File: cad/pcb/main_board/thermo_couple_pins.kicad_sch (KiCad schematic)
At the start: 3 parts

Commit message: Thermo Couple Pins
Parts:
- removed R3, R4: R, symbol Device:R
- removed TC1: 0-60V, symbol Device:Thermocouple_Block
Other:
- added sheet TCPin (tcpin.kicad_sch)
- added sheet TCPin1 (tcpin.kicad_sch)
- added sheet TCPin10 (tcpin.kicad_sch)
- added sheet TCPin11 (tcpin.kicad_sch)
- added sheet TCPin12 (tcpin.kicad_sch)
- added sheet TCPin13 (tcpin.kicad_sch)
- added sheet TCPin14 (tcpin.kicad_sch)
- added sheet TCPin15 (tcpin.kicad_sch)
- added sheet TCPin2 (tcpin.kicad_sch)
- added sheet TCPin3 (tcpin.kicad_sch)
- added sheet TCPin4 (tcpin.kicad_sch)
- added sheet TCPin5 (tcpin.kicad_sch)
- added sheet TCPin6 (tcpin.kicad_sch)
- added sheet TCPin7 (tcpin.kicad_sch)
- added sheet TCPin8 (tcpin.kicad_sch)
- added sheet TCPin9 (tcpin.kicad_sch)
- note removed: "Cap for low pass?"

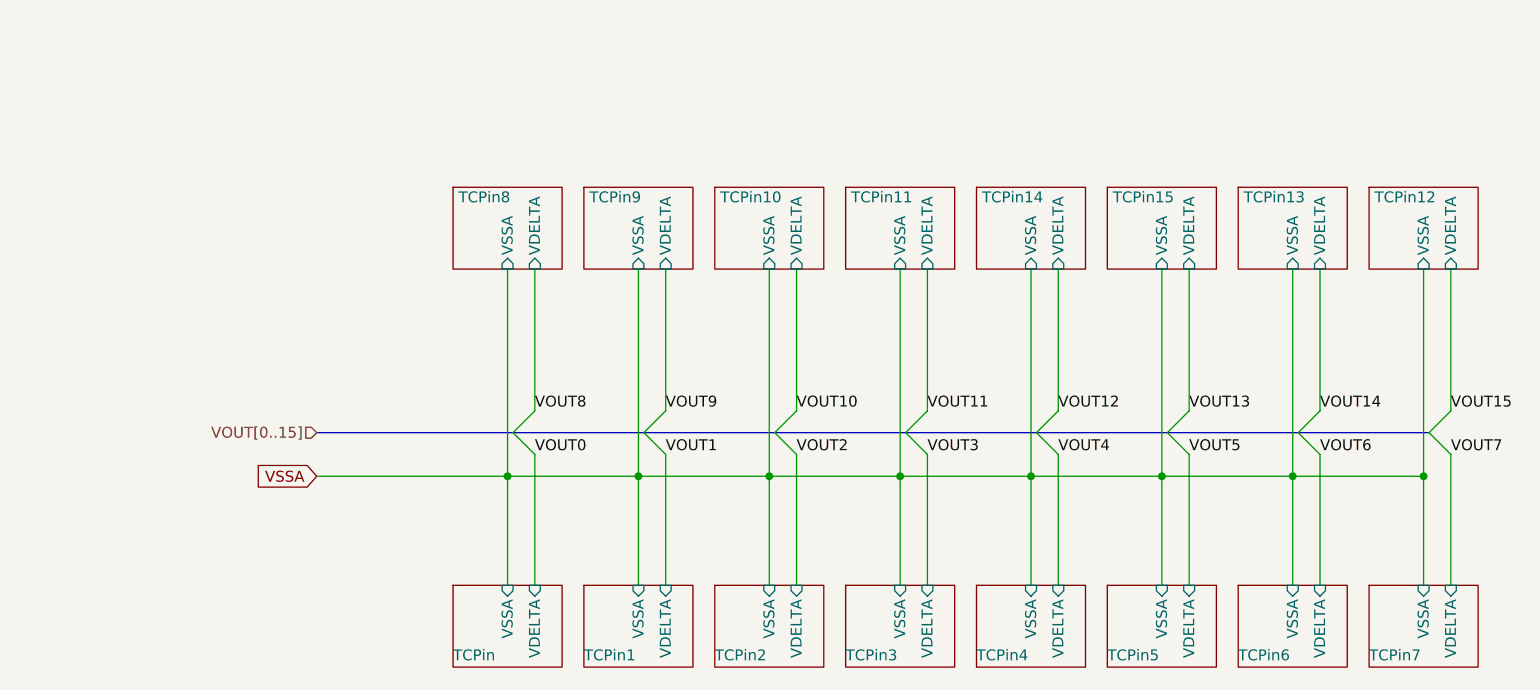
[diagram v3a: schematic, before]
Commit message: Adding JTAG Interface + POGO Pads
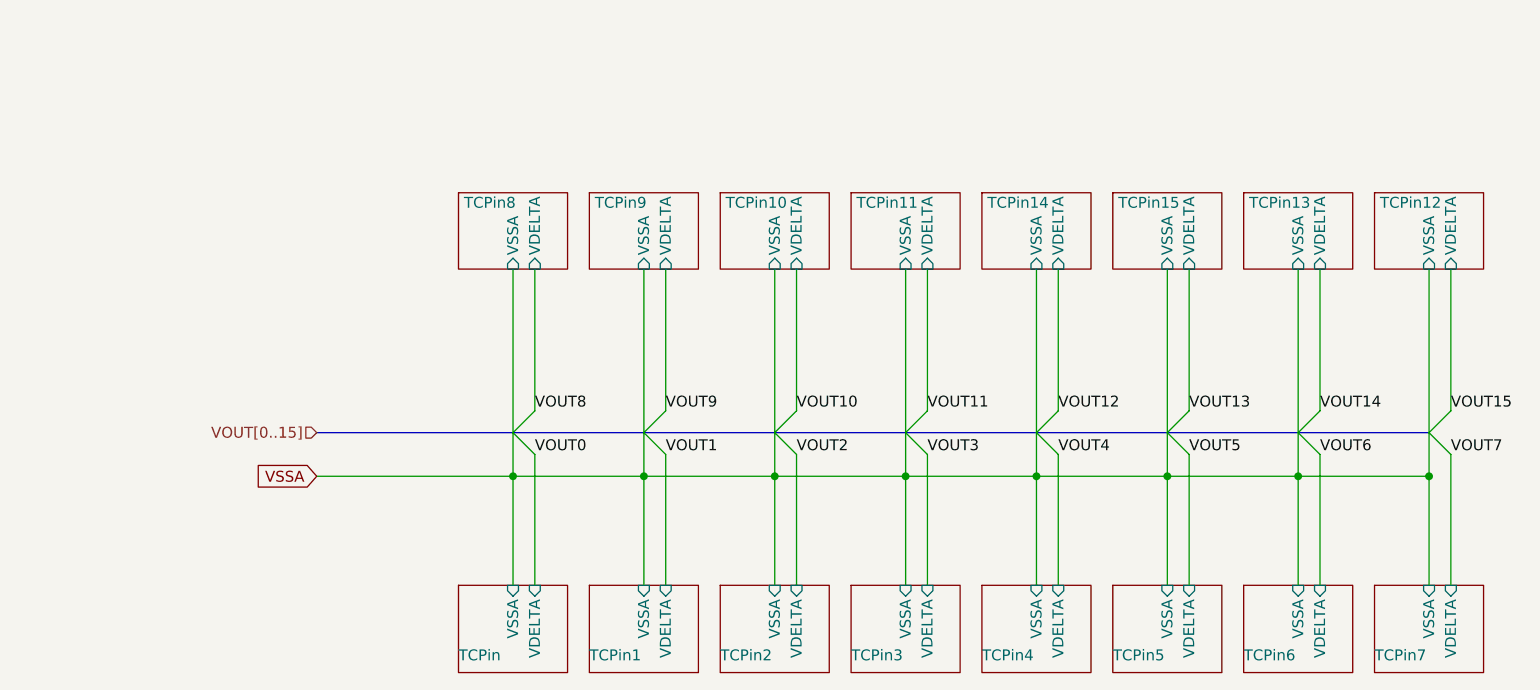
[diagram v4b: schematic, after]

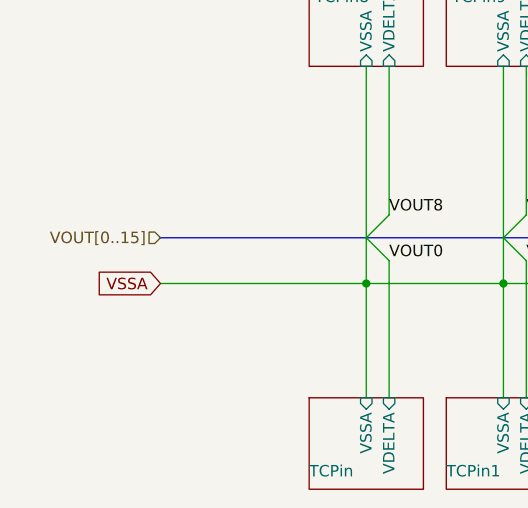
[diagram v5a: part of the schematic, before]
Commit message: DRC mostly checks out now
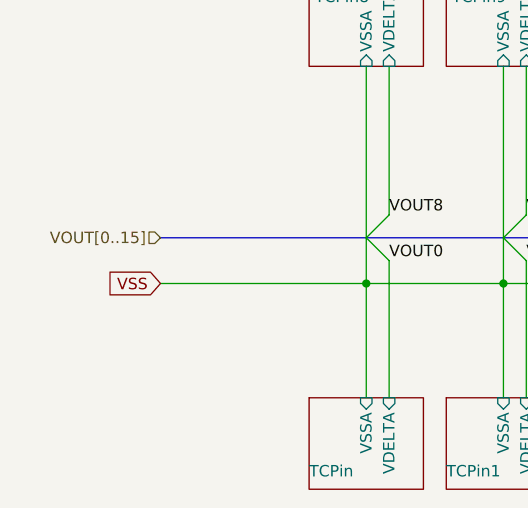
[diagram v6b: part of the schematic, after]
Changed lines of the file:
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@@
 		)
 	)
-	(global_label "VSSA"
+	(global_label "VSS"
 		(shape input)
 		(at 80.01 100.33 180)
@@
 		)
 		(property "Intersheetrefs" "${INTERSHEET_REFS}"
-			(at 72.4286 100.33 0)
+			(at 73.5172 100.33 0)
 			(effects
 				(font
